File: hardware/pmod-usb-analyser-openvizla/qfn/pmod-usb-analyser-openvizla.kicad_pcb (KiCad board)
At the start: 2 copper layers, 31.2 x 41.2 mm, 30 parts, among them J1 PMOD-2x6-MALE, J2 PMOD-2x6-MALE, J3 USB_A, J4 USB_B_Micro, U1 USB3343-CP-TR, Y1 ECS-260-18-33-AGM-TR

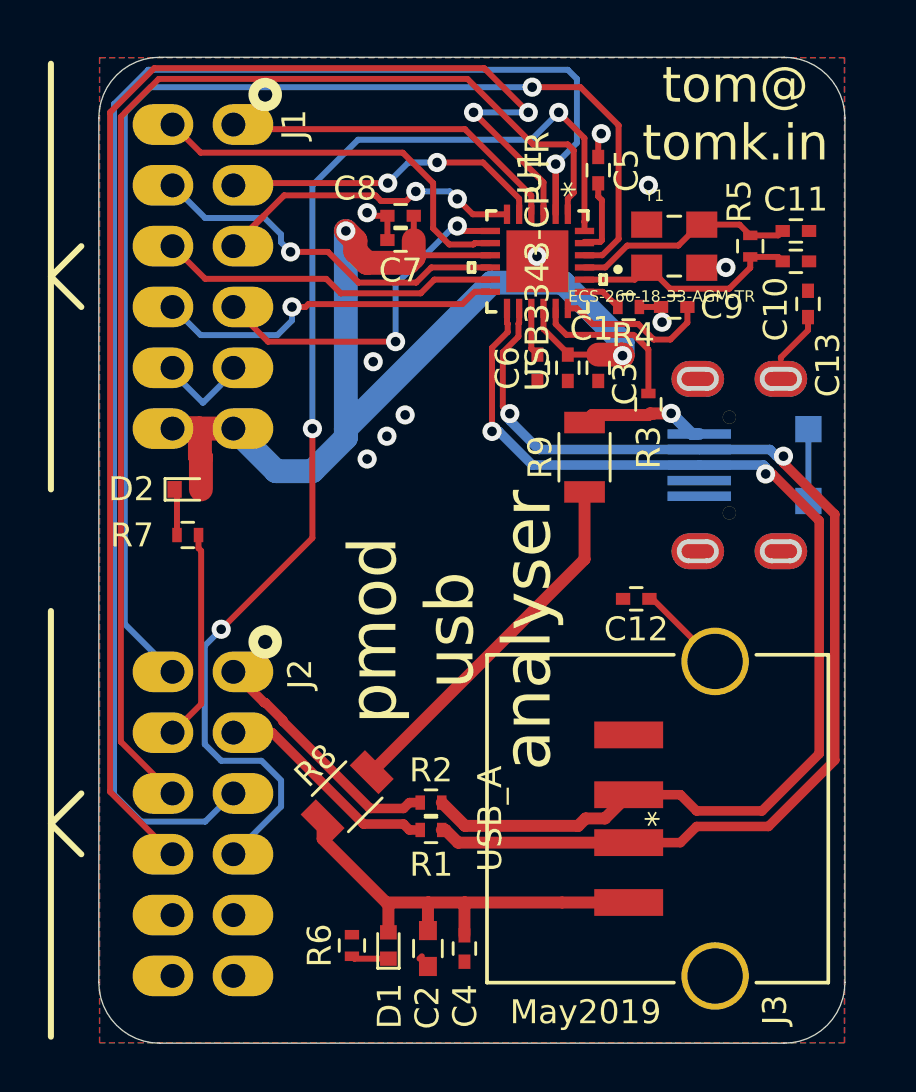
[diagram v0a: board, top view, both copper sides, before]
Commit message: pmod-usb-analyser: feedback from ktempkin - move VBAT to 5V - moved 3.3V to LDO
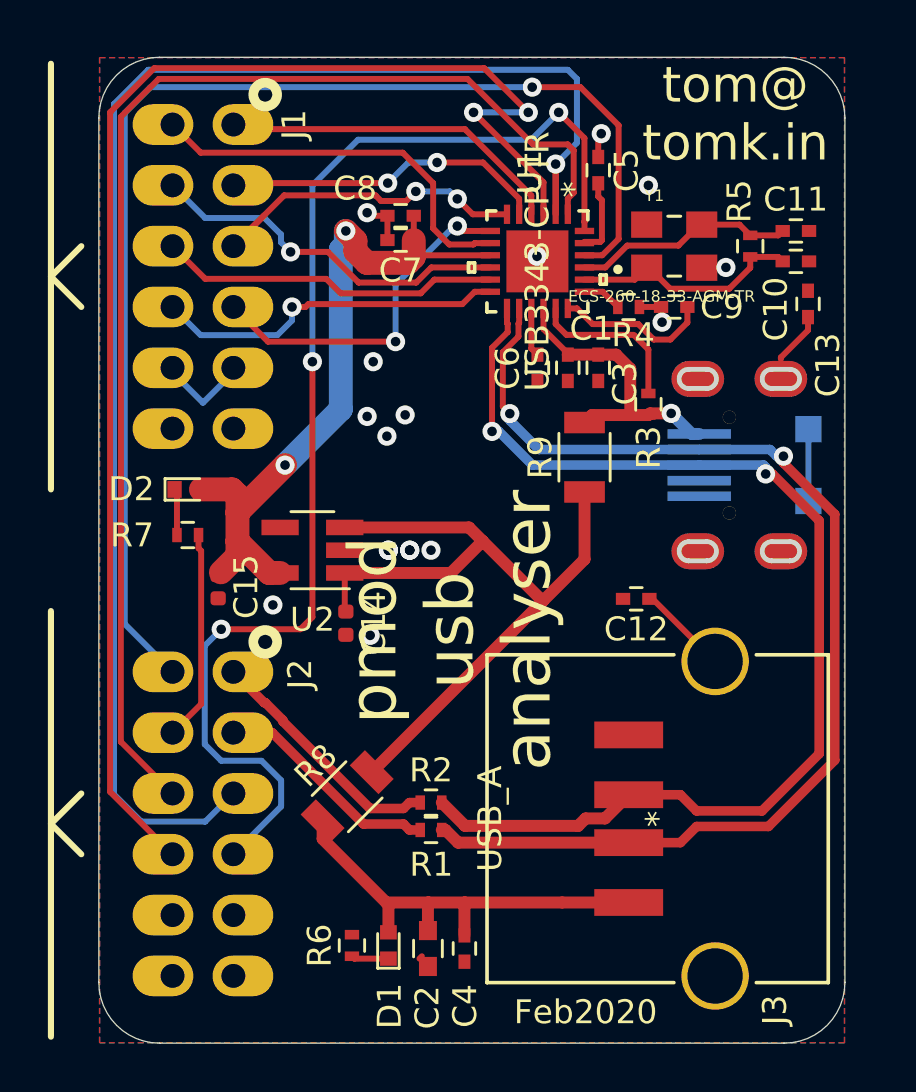
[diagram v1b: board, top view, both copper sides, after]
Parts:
- added C14: 1uF, tom-passives:C_0402_1005Metric, F.Cu at (50.4, 62.7)
- added C15: 1uF, tom-passives:C_0402_1005Metric, F.Cu at (45.1, 61.2)
- added U2: AP2112K-3.3, tom-semiconductors:SOT-23-5_HandSoldering, F.Cu at (49.0, 59.7)
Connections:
- net /VBUS1 renamed VBUS1
- C1 pad 1: +3V3 -> VBUS2
- C3 pad 1: +3V3 -> VBUS2
- J1 pad 12: +3V3 -> Net-(J1-Pad12)
- J1 pad 6: +3V3 -> Net-(J1-Pad6)
- J2 pad 12: (no net) -> Net-(J2-Pad12)
- J2 pad 6: (no net) -> Net-(J2-Pad6)
- J4 pad 4: (no net) -> Net-(J4-Pad4)
- U1 pad 16: +3V3 -> VBUS2
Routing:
- net +3V3: track 51.0 -> 30.3 mm
- net VBUS1: track 15.4 -> 32.9 mm
- net VBUS2: track 5.30 -> 12.4 mm
- net /STP: track 49.9 -> 51.8 mm
- net GND: vias 10 -> 17
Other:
- board text added: "Feb2020"
- board text removed: "May2019"
